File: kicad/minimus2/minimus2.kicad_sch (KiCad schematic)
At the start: 74 parts, among them J1 PROG_SER, J2 LM, J3 LM, Q1 SSM6N58NU_LF, Q2 SSM6N58NU_LF, Q3 DMN3051L, SW1 RESET, SW2 USER_A, SW4 SW_SPDT, U1 LSM6DSRTR, U2 STM32U575CITx, U3 DRV8835, U4 AS5047D, U5 AS5047D, U6 AP2210N-5.0TRG1, U7 AP2210N-3.3TRG1

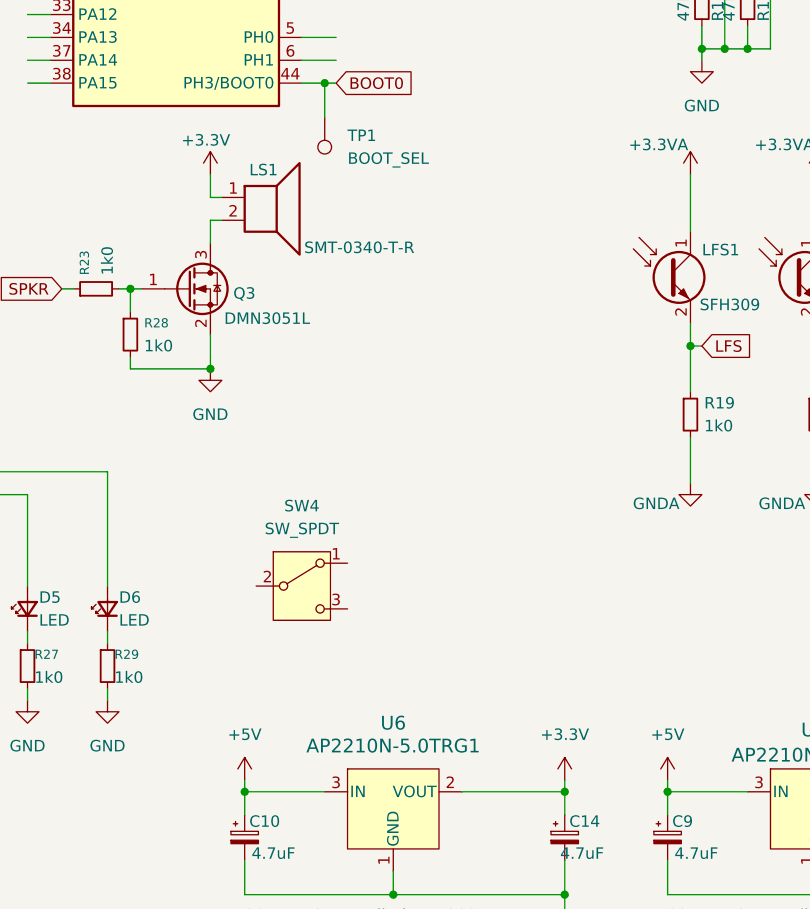
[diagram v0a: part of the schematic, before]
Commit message: update PCB with motors
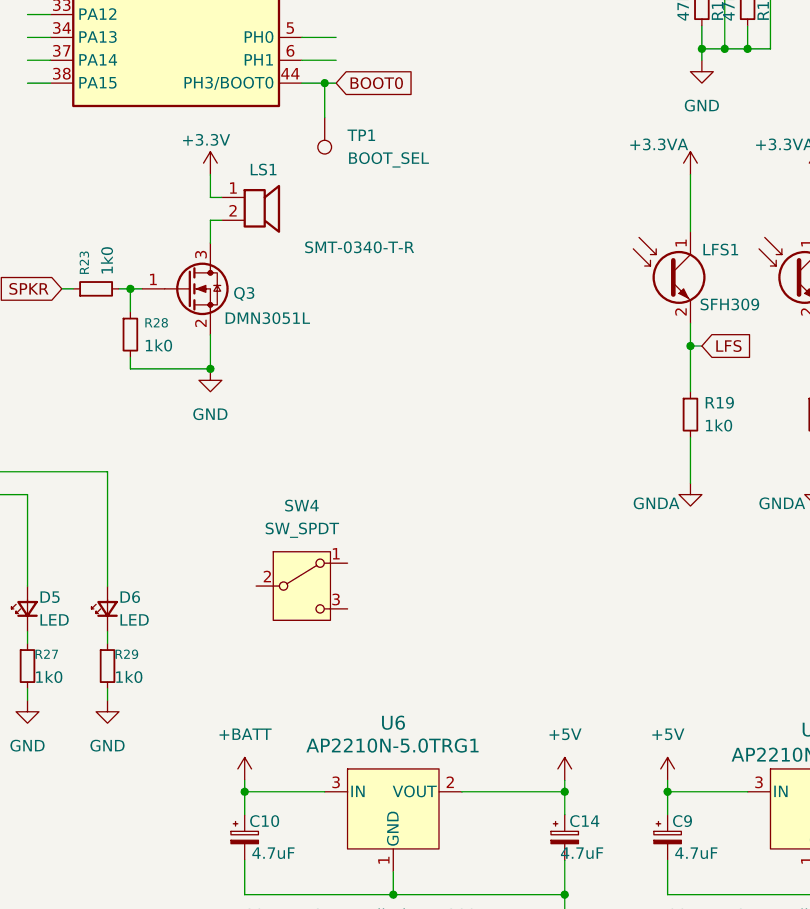
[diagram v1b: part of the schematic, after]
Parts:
- LS1: symbol Device:Speaker -> minimus:Speaker
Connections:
- net +3.3V: no longer C14.1, U6.2 (VOUT)
- net +5V: now also C14.1, U6.2 (VOUT); no longer C10.1, U6.3 (IN)
- net +BATT: now also C10.1, U6.3 (IN)
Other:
- moved on the sheet: LS1
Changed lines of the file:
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@@
 	)
 	(symbol
-		(lib_id "power:+5V")
-		(at 80.01 170.18 0)
-		(unit 1)
-		(exclude_from_sim no)
-		(in_bom yes)
-		(on_board yes)
-		(dnp no)
-		(fields_autoplaced yes)
-		(property "Reference" "#PWR043"
-			(at 80.01 173.99 0)
-			(effects
-				(font
-					(size 1.27 1.27)
-				)
-				(hide yes)
-			)
-		)
-		(property "Value" "+5V"
-			(at 80.01 165.1 0)
-			(effects
-				(font
-					(size 1.27 1.27)
-				)
-			)
-		)
-		(property "Footprint" ""
-			(at 80.01 170.18 0)
-			(effects
-				(font
-					(size 1.27 1.27)
-				)
-				(hide yes)
-			)
-		)
-		(property "Datasheet" ""
-			(at 80.01 170.18 0)
-			(effects
-				(font
-					(size 1.27 1.27)
-				)
-				(hide yes)
-			)
-		)
-		(property "Description" "Power symbol creates a global label with name \"+5V\""
-			(at 80.01 170.18 0)
-			(effects
-				(font
-					(size 1.27 1.27)
-				)
-				(hide yes)
-			)
-		)
-		(pin "1"
-		)
-		(instances
-			(project "minimus2"
-				(path "/5f02052c-d497-4c23-977a-de0c9b1a7969"
-					(reference "#PWR043")
-					(unit 1)
-				)
-			)
-		)
-	)
-	(symbol
 		(lib_id "Sensor_Optical:SFH309")
 		(at 140.97 114.3 0)
@@
 	)
 	(symbol
+		(lib_id "power:+BATT")
+		(at 80.01 170.18 0)
+		(unit 1)
+		(exclude_from_sim no)
+		(in_bom yes)
+		(on_board yes)
+		(dnp no)
+		(fields_autoplaced yes)
+		(property "Reference" "#PWR043"
+			(at 80.01 173.99 0)
+			(effects
+				(font
+					(size 1.27 1.27)
+				)
+				(hide yes)
+			)
+		)
+		(property "Value" "+BATT"
+			(at 80.01 165.1 0)
+			(effects
+				(font
+					(size 1.27 1.27)
+				)
+			)
+		)
+		(property "Footprint" ""
+			(at 80.01 170.18 0)
+			(effects
+				(font
+					(size 1.27 1.27)
+				)
+				(hide yes)
+			)
+		)
+		(property "Datasheet" ""
+			(at 80.01 170.18 0)
+			(effects
+				(font
+					(size 1.27 1.27)
+				)
+				(hide yes)
+			)
+		)
+		(property "Description" "Power symbol creates a global label with name \"+BATT\""
+			(at 80.01 170.18 0)
+			(effects
+				(font
+					(size 1.27 1.27)
+				)
+				(hide yes)
+			)
+		)
+		(pin "1"
+		)
+		(instances
+			(project "minimus2"
+				(path "/5f02052c-d497-4c23-977a-de0c9b1a7969"
+					(reference "#PWR043")
+					(unit 1)
+				)
+			)
+		)
+	)
+	(symbol
 		(lib_id "Device:L")
 		(at 260.35 83.82 90)
@@
 	)
 	(symbol
-		(lib_id "Device:Speaker")
+		(lib_id "minimus:Speaker")
 		(at 82.55 105.41 0)
 		(unit 1)
@@
 	)
 	(symbol
+		(lib_id "power:+5V")
+		(at 115.57 170.18 0)
+		(unit 1)
+		(exclude_from_sim no)
+		(in_bom yes)
+		(on_board yes)
+		(dnp no)
+		(fields_autoplaced yes)
+		(property "Reference" "#PWR044"
+			(at 115.57 173.99 0)
+			(effects
+				(font
+					(size 1.27 1.27)
+				)
+				(hide yes)
+			)
+		)
+		(property "Value" "+5V"
+			(at 115.57 165.1 0)
+			(effects
+				(font
+					(size 1.27 1.27)
+				)
+			)
+		)
+		(property "Footprint" ""
+			(at 115.57 170.18 0)
+			(effects
+				(font
+					(size 1.27 1.27)
+				)
+				(hide yes)
+			)
+		)
+		(property "Datasheet" ""
+			(at 115.57 170.18 0)
+			(effects
+				(font
+					(size 1.27 1.27)
+				)
+				(hide yes)
+			)
+		)
+		(property "Description" "Power symbol creates a global label with name \"+5V\""
+			(at 115.57 170.18 0)
+			(effects
+				(font
+					(size 1.27 1.27)
+				)
+				(hide yes)
+			)
+		)
+		(pin "1"
+		)
+		(instances
+			(project "minimus2"
+				(path "/5f02052c-d497-4c23-977a-de0c9b1a7969"
+					(reference "#PWR044")
+					(unit 1)
+				)
+			)
+		)
+	)
+	(symbol
 		(lib_id "Device:NetTie_2")
 		(at 266.7 154.94 0)
@@
 					(unit 1)
 				)
-			)
-		)
-	)
-	(symbol
-		(lib_id "power:+3.3V")
-		(at 115.57 170.18 0)
-		(unit 1)
-		(exclude_from_sim no)
-		(in_bom yes)
-		(on_board yes)
-		(dnp no)
-		(fields_autoplaced yes)
-		(property "Reference" "#PWR044"
-			(at 115.57 173.99 0)
-			(effects
-				(font
-					(size 1.27 1.27)
-				)
-				(hide yes)
-			)
-		)
-		(property "Value" "+3.3V"
-			(at 115.57 165.1 0)
-			(effects
-				(font
-					(size 1.27 1.27)
-				)
-			)
-		)
-		(property "Footprint" ""
-			(at 115.57 170.18 0)
-			(effects
-				(font
-					(size 1.27 1.27)
-				)
-				(hide yes)
-			)
-		)
-		(property "Datasheet" ""
-			(at 115.57 170.18 0)
-			(effects
-				(font
-					(size 1.27 1.27)
-				)
-				(hide yes)
-			)
-		)
-		(property "Description" "Power symbol creates a global label with name \"+3.3V\""
-			(at 115.57 170.18 0)
-			(effects
-				(font
-					(size 1.27 1.27)
-				)
-				(hide yes)
-			)
-		)
-		(pin "1"
-		)
-		(instances
-			(project "minimus2"
-				(path "/5f02052c-d497-4c23-977a-de0c9b1a7969"
-					(reference "#PWR044")
-					(unit 1)
-				)

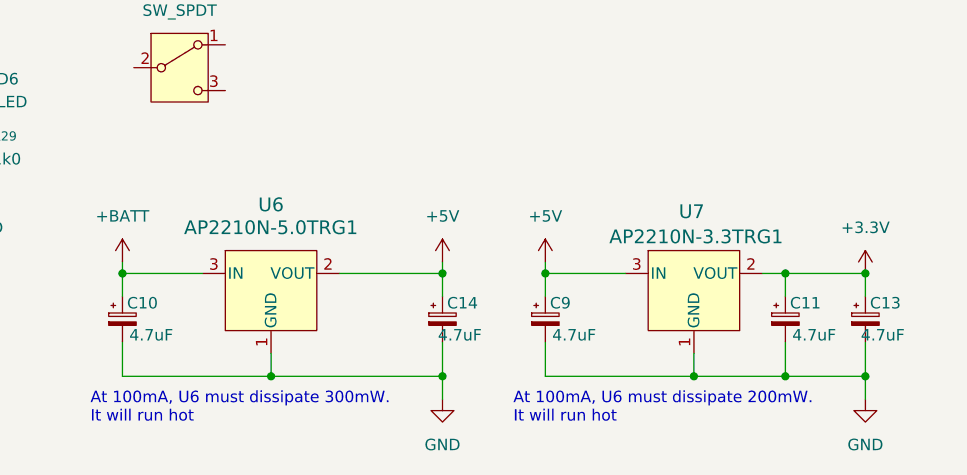
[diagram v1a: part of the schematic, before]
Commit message: update power supply
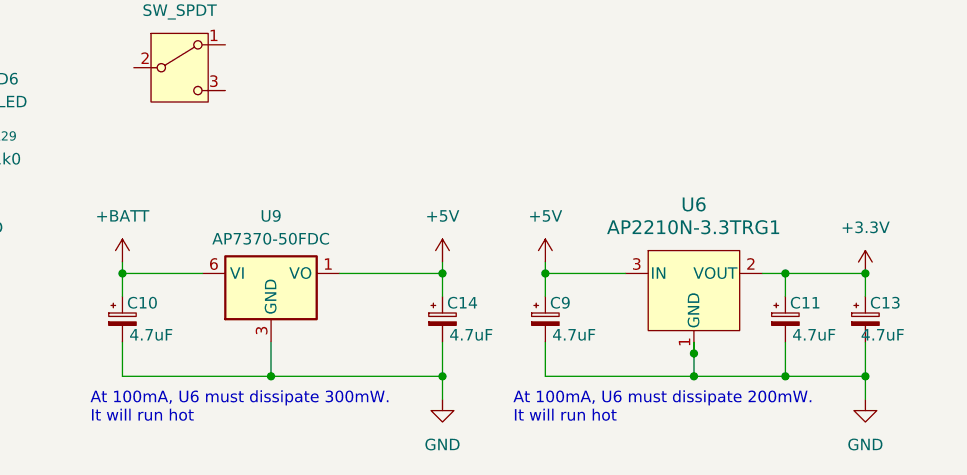
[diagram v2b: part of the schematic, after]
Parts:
- removed U6: AP2210N-5.0TRG1, minimus:AP2210N-x.xTRG1_DIO, symbol minimus:AP2210N-5.0TRG1
- removed U7: AP2210N-3.3TRG1, minimus:AP2210N-x.xTRG1_DIO, symbol minimus:AP2210N-3.3TRG1
- added U6: AP2210N-3.3TRG1, minimus:AP2210N-x.xTRG1_DIO, symbol minimus:AP2210N-3.3TRG1
- added U9: AP7370-50FDC, minimus:DFN-6-1EP_2x2mm_P0.65mm_EP1.01x1.7mm, symbol Regulator_Linear:AP7370-50FDC
- LFE1, LSE1, RFE1, RSE1: footprint LED_THT:LED_D3.0mm_Horizontal_O1.27mm_Z2.0mm_IRBlack -> minimus:LED_D3.0mm_Horizontal_O3.81mm_Z6.0mm
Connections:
- net +3.3V: now also U6.2 (VOUT)
- net +5V: now also U6.3 (IN), U9.1 (VO)
- net +BATT: now also U9.6 (VI)
- net GND: now also U6.1 (GND), U9.3 (GND), U9.7 (GND)
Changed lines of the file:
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@@
 	)
 	(junction
+		(at 143.51 180.34)
+		(diameter 0)
+		(color 0 0 0 0)
+	)
+	(junction
 		(at 25.4 111.76)
 		(diameter 0)
@@
 	(wire
 		(pts
-			(xy 96.52 180.34) (xy 96.52 182.88)
+			(xy 86.36 53.34) (xy 90.17 53.34)
 		)
 		(stroke
@@
 	(wire
 		(pts
-			(xy 86.36 53.34) (xy 90.17 53.34)
+			(xy 86.36 66.04) (xy 90.17 66.04)
 		)
 		(stroke
@@
 	(wire
 		(pts
-			(xy 86.36 66.04) (xy 90.17 66.04)
+			(xy 143.51 180.34) (xy 143.51 182.88)
 		)
 		(stroke
@@
 	(wire
 		(pts
+			(xy 96.52 179.07) (xy 96.52 182.88)
+		)
+		(stroke
+			(width 0)
+			(type default)
+		)
+	)
+	(wire
+		(pts
 			(xy 86.36 87.63) (xy 90.17 87.63)
 		)
@@
 	(wire
 		(pts
-			(xy 143.51 180.34) (xy 143.51 182.88)
+			(xy 143.51 179.07) (xy 143.51 180.34)
 		)
 		(stroke
@@
 			)
 		)
-		(property "Footprint" "LED_THT:LED_D3.0mm_Horizontal_O1.27mm_Z2.0mm_IRBlack"
+		(property "Footprint" "minimus:LED_D3.0mm_Horizontal_O3.81mm_Z6.0mm"
 			(at 135.89 30.48 90)
 			(effects
@@
 	)
 	(symbol
-		(lib_id "minimus:AP2210N-3.3TRG1")
-		(at 143.51 172.72 0)
-		(unit 1)
-		(exclude_from_sim no)
-		(in_bom yes)
-		(on_board yes)
-		(dnp no)
-		(property "Reference" "U7"
-			(at 143.256 164.592 0)
-			(effects
-				(font
-					(size 1.524 1.524)
-				)
-			)
-		)
-		(property "Value" "AP2210N-3.3TRG1"
-			(at 143.764 167.386 0)
-			(effects
-				(font
-					(size 1.524 1.524)
-				)
-			)
-		)
-		(property "Footprint" "minimus:AP2210N-x.xTRG1_DIO"
-			(at 143.51 172.72 0)
-			(effects
-				(font
-					(size 1.27 1.27)
-					(italic yes)
-				)
-				(hide yes)
-			)
-		)
-		(property "Datasheet" "AP2210N-3.3TRG1"
-			(at 143.51 172.72 0)
-			(effects
-				(font
-					(size 1.27 1.27)
-					(italic yes)
-				)
-				(hide yes)
-			)
-		)
-		(property "Description" ""
-			(at 143.51 172.72 0)
-			(effects
-				(font
-					(size 1.27 1.27)
-				)
-				(hide yes)
-			)
-		)
-		(pin "2"
-		)
-		(pin "3"
-		)
-		(pin "1"
-		)
-		(instances
-			(project ""
-				(path "/5f02052c-d497-4c23-977a-de0c9b1a7969"
-					(reference "U7")
-					(unit 1)
-				)
-			)
-		)
-	)
-	(symbol
 		(lib_id "power:+5V")
 		(at 222.25 156.21 0)
@@
 	)
 	(symbol
+		(lib_id "minimus:AP2210N-3.3TRG1")
+		(at 143.51 172.72 0)
+		(unit 1)
+		(exclude_from_sim no)
+		(in_bom yes)
+		(on_board yes)
+		(dnp no)
+		(fields_autoplaced yes)
+		(property "Reference" "U6"
+			(at 143.51 163.83 0)
+			(effects
+				(font
+					(size 1.524 1.524)
+				)
+			)
+		)
+		(property "Value" "AP2210N-3.3TRG1"
+			(at 143.51 166.37 0)
+			(effects
+				(font
+					(size 1.524 1.524)
+				)
+			)
+		)
+		(property "Footprint" "minimus:AP2210N-x.xTRG1_DIO"
+			(at 143.51 172.72 0)
+			(effects
+				(font
+					(size 1.27 1.27)
+					(italic yes)
+				)
+				(hide yes)
+			)
+		)
+		(property "Datasheet" "AP2210N-3.3TRG1"
+			(at 143.51 172.72 0)
+			(effects
+				(font
+					(size 1.27 1.27)
+					(italic yes)
+				)
+				(hide yes)
+			)
+		)
+		(property "Description" "LDO Regulator 3.3V SOT23"
+			(at 143.51 172.72 0)
+			(effects
+				(font
+					(size 1.27 1.27)
+				)
+				(hide yes)
+			)
+		)
+		(pin "2"
+		)
+		(pin "3"
+		)
+		(pin "1"
+		)
+		(instances
+			(project ""
+				(path "/5f02052c-d497-4c23-977a-de0c9b1a7969"
+					(reference "U6")
+					(unit 1)
+				)
+			)
+		)
+	)
+	(symbol
 		(lib_id "power:PWR_FLAG")
 		(at 243.84 156.21 180)
@@
 		)
 		(property "Value" "4.7uF"
-			(at 115.062 178.308 0)
+			(at 116.332 178.308 0)
 			(effects
 				(font
@@
 	)
 	(symbol
-		(lib_id "minimus:AP2210N-5.0TRG1")
-		(at 96.52 172.72 0)
-		(unit 1)
-		(exclude_from_sim no)
-		(in_bom yes)
-		(on_board yes)
-		(dnp no)
-		(fields_autoplaced yes)
-		(property "Reference" "U6"
-			(at 96.52 163.83 0)
-			(effects
-				(font
-					(size 1.524 1.524)
-				)
-			)
-		)
-		(property "Value" "AP2210N-5.0TRG1"
-			(at 96.52 166.37 0)
-			(effects
-				(font
-					(size 1.524 1.524)
-				)
-			)
-		)
-		(property "Footprint" "minimus:AP2210N-x.xTRG1_DIO"
-			(at 96.52 172.72 0)
-			(effects
-				(font
-					(size 1.27 1.27)
-					(italic yes)
-				)
-				(hide yes)
-			)
-		)
-		(property "Datasheet" ""
-			(at 96.52 172.72 0)
-			(effects
-				(font
-					(size 1.27 1.27)
-					(italic yes)
-				)
-				(hide yes)
-			)
-		)
-		(property "Description" "LDO Regulator 5.0V SOT23"
-			(at 96.52 172.72 0)
-			(effects
-				(font
-					(size 1.27 1.27)
-				)
-				(hide yes)
-			)
-		)
-		(pin "1"
-		)
-		(pin "2"
-		)
-		(pin "3"
-		)
-		(instances
-			(project ""
-				(path "/5f02052c-d497-4c23-977a-de0c9b1a7969"
-					(reference "U6")
-					(unit 1)
-				)
-			)
-		)
-	)
-	(symbol
 		(lib_id "power:+BATT")
 		(at 243.84 66.04 0)
@@
 			)
 		)
-		(property "Footprint" "LED_THT:LED_D3.0mm_Horizontal_O1.27mm_Z2.0mm_IRBlack"
+		(property "Footprint" "minimus:LED_D3.0mm_Horizontal_O3.81mm_Z6.0mm"
 			(at 130.81 30.48 90)
 			(effects
@@
 			)
 		)
-		(property "Footprint" "LED_THT:LED_D3.0mm_Horizontal_O1.27mm_Z2.0mm_IRBlack"
+		(property "Footprint" "minimus:LED_D3.0mm_Horizontal_O3.81mm_Z6.0mm"
 			(at 165.1 30.48 90)
 			(effects
@@
 	)
 	(symbol
+		(lib_id "Regulator_Linear:AP7370-50FDC")
+		(at 96.52 171.45 0)
+		(unit 1)
+		(exclude_from_sim no)
+		(in_bom yes)
+		(on_board yes)
+		(dnp no)
+		(fields_autoplaced yes)
+		(property "Reference" "U9"
+			(at 96.52 165.1 0)
+			(effects
+				(font
+					(size 1.27 1.27)
+				)
+			)
+		)
+		(property "Value" "AP7370-50FDC"
+			(at 96.52 167.64 0)
+			(effects
+				(font
+					(size 1.27 1.27)
+				)
+			)
+		)
+		(property "Footprint" "minimus:DFN-6-1EP_2x2mm_P0.65mm_EP1.01x1.7mm"
+			(at 96.52 171.45 0)
+			(effects
+				(font
+					(size 1.27 1.27)
+				)
+				(hide yes)
+			)
+		)
+		(property "Datasheet" "https://www.diodes.com/assets/Datasheets/AP7370.pdf"
+			(at 96.52 171.45 0)
+			(effects
+				(font
+					(size 1.27 1.27)
+				)
+				(hide yes)
+			)
+		)
+		(property "Description" "350mA Low-Dropout Linear Regulator, 5.0V fixed output, DFN-6"
+			(at 96.52 171.45 0)
+			(effects
+				(font
+					(size 1.27 1.27)
+				)
+				(hide yes)
+			)
+		)
+		(property "LCSC" "C6125709"
+			(at 96.52 171.45 0)
+			(effects
+				(font
+					(size 1.27 1.27)
+				)
+				(hide yes)
+			)
+		)
+		(pin "4"
+		)
+		(pin "7"
+		)
+		(pin "3"
+		)
+		(pin "1"
+		)
+		(pin "5"
+		)
+		(pin "2"
+		)
+		(pin "6"
+		)
+		(instances
+			(project ""
+				(path "/5f02052c-d497-4c23-977a-de0c9b1a7969"
+					(reference "U9")
+					(unit 1)
+				)
+			)
+		)
+	)
+	(symbol
 		(lib_id "power:GND")
 		(at 64.77 161.29 0)
@@
 			)
 		)
-		(property "Footprint" "LED_THT:LED_D3.0mm_Horizontal_O1.27mm_Z2.0mm_IRBlack"
+		(property "Footprint" "minimus:LED_D3.0mm_Horizontal_O3.81mm_Z6.0mm"
 			(at 170.18 30.48 90)
 			(effects

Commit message: update EDA
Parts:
- added C12, C15: 100nF, Capacitor_SMD:C_0402_1005Metric, symbol minimus:C_Small
- added R15, R17, R18, R30, R32, R33: 47k, Resistor_SMD:R_0402_1005Metric, symbol Device:R_Small
- C1, C10, C11, C13, C14, C2, C3, C4, C5, C6, C7, C8, C9, D2, D3, D4, D5, D6, J2, J3, L1, L2, LFE1, LFS1, LSE1, LSS1, R1, R10, R11, R12, R13, R14, R16, R19, R2, R20, R21, R22, R23, R24, R25, R26, R27, R28, R29, R3, R31, R4, R5, R6, R7, R8, R9, RFE1, RFS1, RSE1, RSS1, SW1, SW2, SW4, TP1, U2, U6: Digikey (none) -> -; LCSC (none) -> -
- J1: LCSC (none) -> -
- LS1, Q3, U1, U9: Digikey (none) -> -
- Q1, Q2: Digikey (none) -> -; LCSC (none) -> C262142
- U4, U5: symbol Sensor_Magnetic:AS5047D -> minimus:AS5047D; Digikey (none) -> -; LCSC (none) -> -
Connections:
- net +3.3V: now also U4.11 (VDD), U4.12 (VDD3V3), U5.11 (VDD), U5.12 (VDD3V3), C12.1, C15.1, R15.1, R17.1
- net GND: now also U4.5 (TST), U5.5 (TST), C12.2, C15.2, R18.2, R30.2, R32.2, R33.2
- net at U4.1 (~{CS}): now also R15.2
- net at U4.2 (CLK): now also R33.1
- net at U4.4 (MOSI): now also R32.1
- net LENC_B: now reaches U4.6 (B)
- net LENC_A: now reaches U4.7 (A)
- net at U5.1 (~{CS}): now also R17.2
- net at U5.2 (CLK): now also R30.1
- net at U5.4 (MOSI): now also R18.1
- net RENC_B: now reaches U5.6 (B)
- net RENC_A: now reaches U5.7 (A)
- no-connect marks 1 -> 9
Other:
- moved on the sheet: J1, J2, J3, L1, L2, LFE1, LFS1, LSE1, LSS1, Q1, Q2, R1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
